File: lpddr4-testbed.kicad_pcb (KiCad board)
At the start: 6 copper layers, 69.6 x 30 mm, 68 parts, among them IC1 PCA96408APW, IC2 AT24CS01, J1 ddr4-sodimm-edge-connector, U1 MT53E1G32D2NP-046, U2 TPS613221ADBVT

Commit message: Replace broken component -PCA6408APW
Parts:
- IC1: value PCA96408APW -> PCA6408APW

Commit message: Migrate to KiCad 6
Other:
- net class Default removed

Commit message: Clean DRC
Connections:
- IC1 pad 11: Net-(IC1-Pad11) -> unconnected-(IC1-Pad11)
- IC1 pad 12: Net-(IC1-Pad12) -> unconnected-(IC1-Pad12)
- IC1 pad 13: Net-(IC1-Pad13) -> unconnected-(IC1-Pad13)
- J1 pad 100: Net-(J1-Pad100) -> unconnected-(J1-Pad100)
- J1 pad 102: Net-(J1-Pad102) -> unconnected-(J1-Pad102)
- J1 pad 104: Net-(J1-Pad104) -> unconnected-(J1-Pad104)
- J1 pad 106: Net-(J1-Pad106) -> unconnected-(J1-Pad106)
- J1 pad 108: Net-(J1-Pad108) -> unconnected-(J1-Pad108)
- J1 pad 109: Net-(J1-Pad109) -> unconnected-(J1-Pad109)
- J1 pad 110: Net-(J1-Pad110) -> unconnected-(J1-Pad110)
- J1 pad 111: Net-(J1-Pad111) -> unconnected-(J1-Pad111)
- J1 pad 112: Net-(J1-Pad112) -> unconnected-(J1-Pad112)
- J1 pad 113: Net-(J1-Pad113) -> unconnected-(J1-Pad113)
- J1 pad 114: Net-(J1-Pad114) -> unconnected-(J1-Pad114)
- J1 pad 115: Net-(J1-Pad115) -> unconnected-(J1-Pad115)
- J1 pad 117: Net-(J1-Pad117) -> unconnected-(J1-Pad117)
- J1 pad 119: Net-(J1-Pad119) -> unconnected-(J1-Pad119)
- J1 pad 121: Net-(J1-Pad121) -> unconnected-(J1-Pad121)
- J1 pad 123: Net-(J1-Pad123) -> unconnected-(J1-Pad123)
- J1 pad 125: Net-(J1-Pad125) -> unconnected-(J1-Pad125)
- J1 pad 131: Net-(J1-Pad131) -> unconnected-(J1-Pad131)
- J1 pad 132: Net-(J1-Pad132) -> unconnected-(J1-Pad132)
- J1 pad 133: Net-(J1-Pad133) -> unconnected-(J1-Pad133)
- J1 pad 134: Net-(J1-Pad134) -> unconnected-(J1-Pad134)
- J1 pad 135: Net-(J1-Pad135) -> unconnected-(J1-Pad135)
- J1 pad 136: Net-(J1-Pad136) -> unconnected-(J1-Pad136)
- J1 pad 137: Net-(J1-Pad137) -> unconnected-(J1-Pad137)
- J1 pad 138: Net-(J1-Pad138) -> unconnected-(J1-Pad138)
- J1 pad 139: Net-(J1-Pad139) -> unconnected-(J1-Pad139)
- J1 pad 140: Net-(J1-Pad140) -> unconnected-(J1-Pad140)
- J1 pad 141: Net-(J1-Pad141) -> unconnected-(J1-Pad141)
- J1 pad 142: Net-(J1-Pad142) -> unconnected-(J1-Pad142)
- J1 pad 143: Net-(J1-Pad143) -> unconnected-(J1-Pad143)
- J1 pad 144: Net-(J1-Pad144) -> unconnected-(J1-Pad144)
- J1 pad 145: Net-(J1-Pad145) -> unconnected-(J1-Pad145)
- J1 pad 146: Net-(J1-Pad146) -> unconnected-(J1-Pad146)
- J1 pad 147: Net-(J1-Pad147) -> unconnected-(J1-Pad147)
- J1 pad 148: Net-(J1-Pad148) -> unconnected-(J1-Pad148)
- J1 pad 149: Net-(J1-Pad149) -> unconnected-(J1-Pad149)
- J1 pad 150: Net-(J1-Pad150) -> unconnected-(J1-Pad150)
- J1 pad 151: Net-(J1-Pad151) -> unconnected-(J1-Pad151)
- J1 pad 152: Net-(J1-Pad152) -> unconnected-(J1-Pad152)
- J1 pad 153: Net-(J1-Pad153) -> unconnected-(J1-Pad153)
- J1 pad 155: Net-(J1-Pad155) -> unconnected-(J1-Pad155)
- J1 pad 157: Net-(J1-Pad157) -> unconnected-(J1-Pad157)
- J1 pad 159: Net-(J1-Pad159) -> unconnected-(J1-Pad159)
- J1 pad 170: Net-(J1-Pad170) -> unconnected-(J1-Pad170)
- J1 pad 172: Net-(J1-Pad172) -> unconnected-(J1-Pad172)
- J1 pad 174: Net-(J1-Pad174) -> unconnected-(J1-Pad174)
- J1 pad 176: Net-(J1-Pad176) -> unconnected-(J1-Pad176)
- J1 pad 178: Net-(J1-Pad178) -> unconnected-(J1-Pad178)
- J1 pad 180: Net-(J1-Pad180) -> unconnected-(J1-Pad180)
- J1 pad 182: Net-(J1-Pad182) -> unconnected-(J1-Pad182)
- J1 pad 188: Net-(J1-Pad188) -> unconnected-(J1-Pad188)
- J1 pad 190: Net-(J1-Pad190) -> unconnected-(J1-Pad190)
- J1 pad 198: Net-(J1-Pad198) -> unconnected-(J1-Pad198)
- J1 pad 202: Net-(J1-Pad202) -> unconnected-(J1-Pad202)
- J1 pad 208: Net-(J1-Pad208) -> unconnected-(J1-Pad208)
- J1 pad 212: Net-(J1-Pad212) -> unconnected-(J1-Pad212)
- J1 pad 213: Net-(J1-Pad213) -> unconnected-(J1-Pad213)
- J1 pad 214: Net-(J1-Pad214) -> unconnected-(J1-Pad214)
- J1 pad 215: Net-(J1-Pad215) -> unconnected-(J1-Pad215)
- J1 pad 216: Net-(J1-Pad216) -> unconnected-(J1-Pad216)
- J1 pad 217: Net-(J1-Pad217) -> unconnected-(J1-Pad217)
- J1 pad 218: Net-(J1-Pad218) -> unconnected-(J1-Pad218)
- J1 pad 219: Net-(J1-Pad219) -> unconnected-(J1-Pad219)
- J1 pad 220: Net-(J1-Pad220) -> unconnected-(J1-Pad220)
- J1 pad 221: Net-(J1-Pad221) -> unconnected-(J1-Pad221)
- J1 pad 222: Net-(J1-Pad222) -> unconnected-(J1-Pad222)
- J1 pad 223: Net-(J1-Pad223) -> unconnected-(J1-Pad223)
- J1 pad 224: Net-(J1-Pad224) -> unconnected-(J1-Pad224)
- J1 pad 225: Net-(J1-Pad225) -> unconnected-(J1-Pad225)
- J1 pad 226: Net-(J1-Pad226) -> unconnected-(J1-Pad226)
- J1 pad 227: Net-(J1-Pad227) -> unconnected-(J1-Pad227)
- J1 pad 228: Net-(J1-Pad228) -> unconnected-(J1-Pad228)
- J1 pad 229: Net-(J1-Pad229) -> unconnected-(J1-Pad229)
- J1 pad 230: Net-(J1-Pad230) -> unconnected-(J1-Pad230)
- J1 pad 231: Net-(J1-Pad231) -> unconnected-(J1-Pad231)
- J1 pad 232: Net-(J1-Pad232) -> unconnected-(J1-Pad232)
- J1 pad 233: Net-(J1-Pad233) -> unconnected-(J1-Pad233)
- J1 pad 234: Net-(J1-Pad234) -> unconnected-(J1-Pad234)
- J1 pad 235: Net-(J1-Pad235) -> unconnected-(J1-Pad235)
- J1 pad 236: Net-(J1-Pad236) -> unconnected-(J1-Pad236)
- J1 pad 237: Net-(J1-Pad237) -> unconnected-(J1-Pad237)
- J1 pad 238: Net-(J1-Pad238) -> unconnected-(J1-Pad238)
- J1 pad 239: Net-(J1-Pad239) -> unconnected-(J1-Pad239)
- J1 pad 240: Net-(J1-Pad240) -> unconnected-(J1-Pad240)
- J1 pad 241: Net-(J1-Pad241) -> unconnected-(J1-Pad241)
- J1 pad 242: Net-(J1-Pad242) -> unconnected-(J1-Pad242)
- J1 pad 243: Net-(J1-Pad243) -> unconnected-(J1-Pad243)
- J1 pad 244: Net-(J1-Pad244) -> unconnected-(J1-Pad244)
- J1 pad 245: Net-(J1-Pad245) -> unconnected-(J1-Pad245)
- J1 pad 247: Net-(J1-Pad247) -> unconnected-(J1-Pad247)
- J1 pad 249: Net-(J1-Pad249) -> unconnected-(J1-Pad249)
- J1 pad 251: Net-(J1-Pad251) -> unconnected-(J1-Pad251)
- J1 pad 252: Net-(J1-Pad252) -> unconnected-(J1-Pad252)
- J1 pad 253: Net-(J1-Pad253) -> unconnected-(J1-Pad253)
- J1 pad 254: Net-(J1-Pad254) -> unconnected-(J1-Pad254)
- J1 pad 255: Net-(J1-Pad255) -> unconnected-(J1-Pad255)
- J1 pad 256: Net-(J1-Pad256) -> unconnected-(J1-Pad256)
- J1 pad 257: Net-(J1-Pad257) -> unconnected-(J1-Pad257)
- J1 pad 258: Net-(J1-Pad258) -> unconnected-(J1-Pad258)
- J1 pad 259: Net-(J1-Pad259) -> unconnected-(J1-Pad259)
- J1 pad 260: Net-(J1-Pad260) -> unconnected-(J1-Pad260)
- J1 pad 51: Net-(J1-Pad51) -> unconnected-(J1-Pad51)
- J1 pad 52: Net-(J1-Pad52) -> unconnected-(J1-Pad52)
- J1 pad 53: Net-(J1-Pad53) -> unconnected-(J1-Pad53)
- J1 pad 54: Net-(J1-Pad54) -> unconnected-(J1-Pad54)
- J1 pad 55: Net-(J1-Pad55) -> unconnected-(J1-Pad55)
- J1 pad 56: Net-(J1-Pad56) -> unconnected-(J1-Pad56)
- J1 pad 57: Net-(J1-Pad57) -> unconnected-(J1-Pad57)
- J1 pad 58: Net-(J1-Pad58) -> unconnected-(J1-Pad58)
- J1 pad 59: Net-(J1-Pad59) -> unconnected-(J1-Pad59)
- J1 pad 60: Net-(J1-Pad60) -> unconnected-(J1-Pad60)
- J1 pad 61: Net-(J1-Pad61) -> unconnected-(J1-Pad61)
- J1 pad 62: Net-(J1-Pad62) -> unconnected-(J1-Pad62)
- J1 pad 63: Net-(J1-Pad63) -> unconnected-(J1-Pad63)
- J1 pad 64: Net-(J1-Pad64) -> unconnected-(J1-Pad64)
- J1 pad 65: Net-(J1-Pad65) -> unconnected-(J1-Pad65)
- J1 pad 66: Net-(J1-Pad66) -> unconnected-(J1-Pad66)
- J1 pad 67: Net-(J1-Pad67) -> unconnected-(J1-Pad67)
- J1 pad 68: Net-(J1-Pad68) -> unconnected-(J1-Pad68)
- J1 pad 69: Net-(J1-Pad69) -> unconnected-(J1-Pad69)
- J1 pad 70: Net-(J1-Pad70) -> unconnected-(J1-Pad70)
- J1 pad 71: Net-(J1-Pad71) -> unconnected-(J1-Pad71)
- J1 pad 72: Net-(J1-Pad72) -> unconnected-(J1-Pad72)
- J1 pad 73: Net-(J1-Pad73) -> unconnected-(J1-Pad73)
- J1 pad 74: Net-(J1-Pad74) -> unconnected-(J1-Pad74)
- J1 pad 75: Net-(J1-Pad75) -> unconnected-(J1-Pad75)
- J1 pad 76: Net-(J1-Pad76) -> unconnected-(J1-Pad76)
- J1 pad 77: Net-(J1-Pad77) -> unconnected-(J1-Pad77)
- J1 pad 78: Net-(J1-Pad78) -> unconnected-(J1-Pad78)
- J1 pad 79: Net-(J1-Pad79) -> unconnected-(J1-Pad79)
- J1 pad 80: Net-(J1-Pad80) -> unconnected-(J1-Pad80)
- J1 pad 81: Net-(J1-Pad81) -> unconnected-(J1-Pad81)
- J1 pad 82: Net-(J1-Pad82) -> unconnected-(J1-Pad82)
- J1 pad 83: Net-(J1-Pad83) -> unconnected-(J1-Pad83)
- J1 pad 84: Net-(J1-Pad84) -> unconnected-(J1-Pad84)
- J1 pad 85: Net-(J1-Pad85) -> unconnected-(J1-Pad85)
- J1 pad 86: Net-(J1-Pad86) -> unconnected-(J1-Pad86)
- J1 pad 87: Net-(J1-Pad87) -> unconnected-(J1-Pad87)
- J1 pad 88: Net-(J1-Pad88) -> unconnected-(J1-Pad88)
- J1 pad 89: Net-(J1-Pad89) -> unconnected-(J1-Pad89)
- J1 pad 90: Net-(J1-Pad90) -> unconnected-(J1-Pad90)
- J1 pad 91: Net-(J1-Pad91) -> unconnected-(J1-Pad91)
- J1 pad 92: Net-(J1-Pad92) -> unconnected-(J1-Pad92)
- J1 pad 94: Net-(J1-Pad94) -> unconnected-(J1-Pad94)
- J1 pad 96: Net-(J1-Pad96) -> unconnected-(J1-Pad96)
- J1 pad 98: Net-(J1-Pad98) -> unconnected-(J1-Pad98)
- U1 pad A1: Net-(U1-PadA1) -> unconnected-(U1-PadA1)
- U1 pad A11: Net-(U1-PadA11) -> unconnected-(U1-PadA11)
- U1 pad A12: Net-(U1-PadA12) -> unconnected-(U1-PadA12)
- U1 pad A2: Net-(U1-PadA2) -> unconnected-(U1-PadA2)
- U1 pad A8: Net-(U1-PadA8) -> unconnected-(U1-PadA8)
- U1 pad AA1: Net-(U1-PadAA1) -> unconnected-(U1-PadAA1)
- U1 pad AA11: Net-(U1-PadAA11) -> unconnected-(U1-PadAA11)
- U1 pad AA12: Net-(U1-PadAA12) -> unconnected-(U1-PadAA12)
- U1 pad AA2: Net-(U1-PadAA2) -> unconnected-(U1-PadAA2)
- U1 pad AA4: Net-(U1-PadAA4) -> unconnected-(U1-PadAA4)
- U1 pad AA9: Net-(U1-PadAA9) -> unconnected-(U1-PadAA9)
- U1 pad AB1: Net-(U1-PadAB1) -> unconnected-(U1-PadAB1)
- U1 pad AB11: Net-(U1-PadAB11) -> unconnected-(U1-PadAB11)
- U1 pad AB12: Net-(U1-PadAB12) -> unconnected-(U1-PadAB12)
- U1 pad AB2: Net-(U1-PadAB2) -> unconnected-(U1-PadAB2)
- U1 pad B1: Net-(U1-PadB1) -> unconnected-(U1-PadB1)
- U1 pad B12: Net-(U1-PadB12) -> unconnected-(U1-PadB12)
- U1 pad G11: Net-(U1-PadG11) -> unconnected-(U1-PadG11)
- U1 pad H3: Net-(U1-PadH3) -> unconnected-(U1-PadH3)
- U1 pad J5: Net-(U1-PadJ5) -> unconnected-(U1-PadJ5)
- U1 pad K5: Net-(U1-PadK5) -> unconnected-(U1-PadK5)
- U1 pad K8: Net-(U1-PadK8) -> unconnected-(U1-PadK8)
- U1 pad N5: Net-(U1-PadN5) -> unconnected-(U1-PadN5)
- U1 pad N8: Net-(U1-PadN8) -> unconnected-(U1-PadN8)
- U1 pad P11: Net-(U1-PadP11) -> unconnected-(U1-PadP11)
- U1 pad P2: Net-(U1-PadP2) -> unconnected-(U1-PadP2)
- U1 pad P4: Net-(U1-PadP4) -> unconnected-(U1-PadP4)
- U1 pad P5: Net-(U1-PadP5) -> unconnected-(U1-PadP5)
- U1 pad P8: Net-(U1-PadP8) -> unconnected-(U1-PadP8)
- U1 pad P9: Net-(U1-PadP9) -> unconnected-(U1-PadP9)
- U1 pad R10: Net-(U1-PadR10) -> unconnected-(U1-PadR10)
- U1 pad R11: Net-(U1-PadR11) -> unconnected-(U1-PadR11)
- U1 pad R2: Net-(U1-PadR2) -> unconnected-(U1-PadR2)
- U1 pad R3: Net-(U1-PadR3) -> unconnected-(U1-PadR3)
- U1 pad R9: Net-(U1-PadR9) -> unconnected-(U1-PadR9)
- U1 pad U11: Net-(U1-PadU11) -> unconnected-(U1-PadU11)
- U1 pad U2: Net-(U1-PadU2) -> unconnected-(U1-PadU2)
- U1 pad U4: Net-(U1-PadU4) -> unconnected-(U1-PadU4)
- U1 pad U9: Net-(U1-PadU9) -> unconnected-(U1-PadU9)
- U1 pad V10: Net-(U1-PadV10) -> unconnected-(U1-PadV10)
- U1 pad V11: Net-(U1-PadV11) -> unconnected-(U1-PadV11)
- U1 pad V2: Net-(U1-PadV2) -> unconnected-(U1-PadV2)
- U1 pad V3: Net-(U1-PadV3) -> unconnected-(U1-PadV3)
- U1 pad V4: Net-(U1-PadV4) -> unconnected-(U1-PadV4)
- U1 pad V9: Net-(U1-PadV9) -> unconnected-(U1-PadV9)
- U1 pad W10: Net-(U1-PadW10) -> unconnected-(U1-PadW10)
- U1 pad W3: Net-(U1-PadW3) -> unconnected-(U1-PadW3)
- U1 pad Y10: Net-(U1-PadY10) -> unconnected-(U1-PadY10)
- U1 pad Y11: Net-(U1-PadY11) -> unconnected-(U1-PadY11)
- U1 pad Y2: Net-(U1-PadY2) -> unconnected-(U1-PadY2)
- U1 pad Y3: Net-(U1-PadY3) -> unconnected-(U1-PadY3)
- U1 pad Y4: Net-(U1-PadY4) -> unconnected-(U1-PadY4)
- U1 pad Y9: Net-(U1-PadY9) -> unconnected-(U1-PadY9)
- U2 pad 3: Net-(U2-Pad3) -> unconnected-(U2-Pad3)
- U2 pad 5: Net-(U2-Pad5) -> unconnected-(U2-Pad5)
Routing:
- net VDDQ: track 44.7 -> 39.1 mm
- net VDD2: track 57.0 -> 55.6 mm
- net GND: track 237.4 -> 236.3 mm
- net VDD1: track 100.3 -> 100.2 mm, vias 19 -> 18

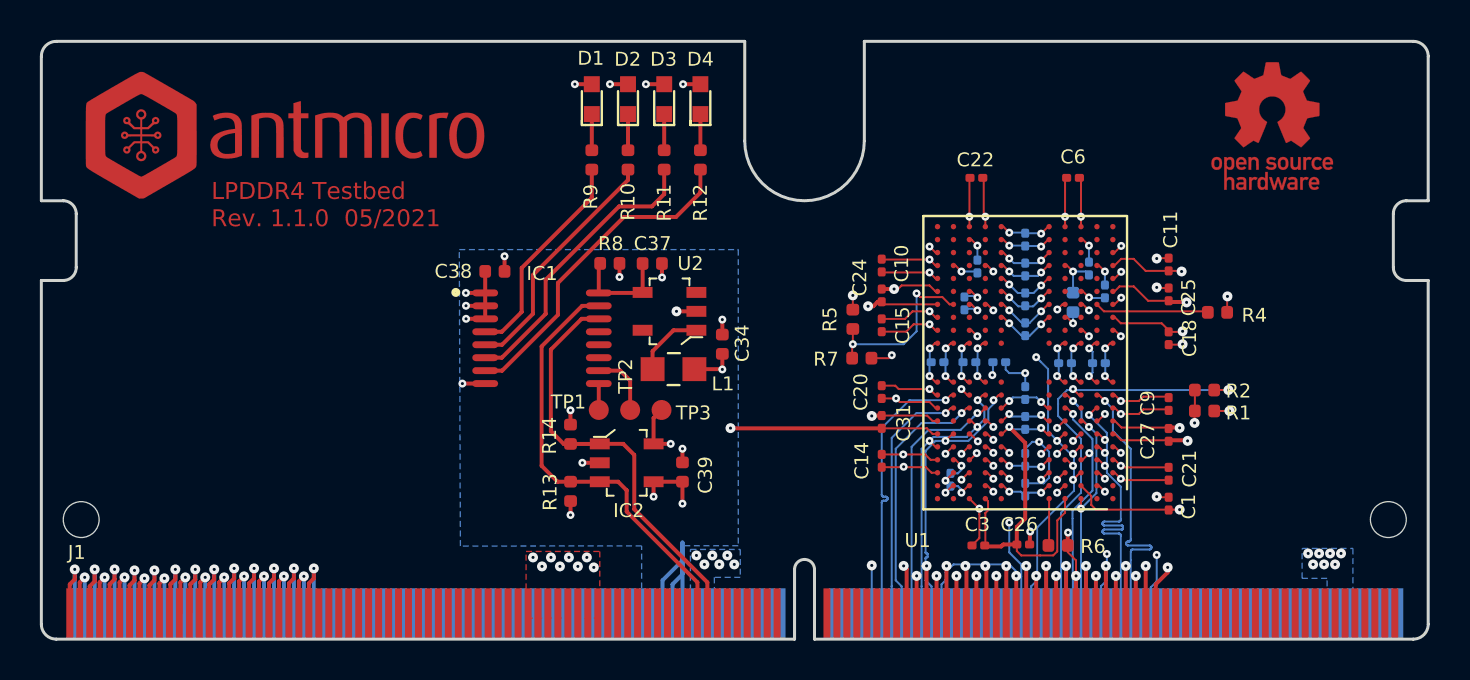
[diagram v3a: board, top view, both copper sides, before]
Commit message: Replace burried vias with regular vias
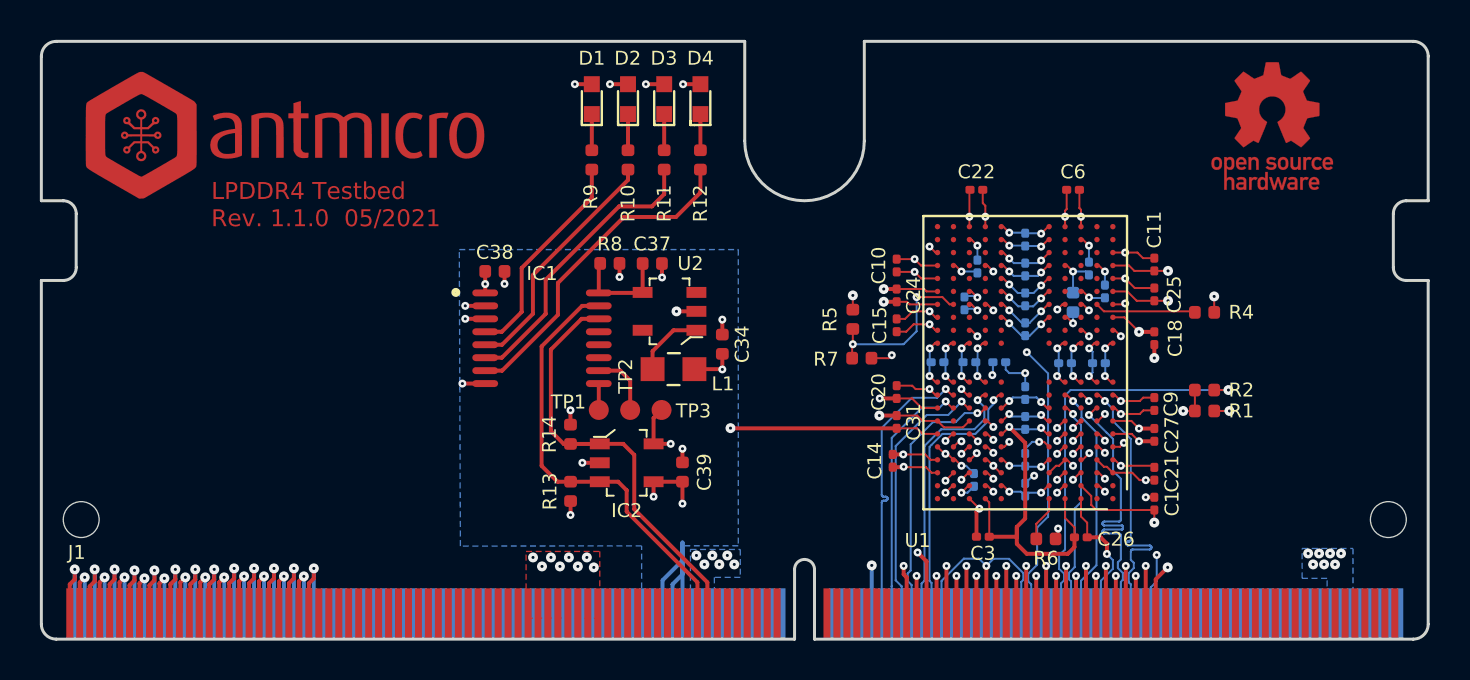
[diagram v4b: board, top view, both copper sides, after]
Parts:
- moved C26 2.91 mm to (152.2, 94.9)
- moved C7 1.18 mm to (146.8, 92.0)
- moved C10 0.75 mm to (142.9, 81.2)
- moved C15 0.75 mm to (142.9, 84.2)
- moved C20 0.75 mm to (142.9, 87.6)
- moved C24 0.75 mm to (142.9, 82.8)
- moved C31 0.75 mm to (142.9, 89.1)
- moved C1 0.72 mm to (155.9, 93.2)
- moved C11 0.72 mm to (155.9, 81.2)
- moved C18 0.72 mm to (155.9, 84.9)
- moved C21 0.72 mm to (155.9, 91.7)
- moved C25 0.72 mm to (155.9, 82.7)
- moved C27 0.72 mm to (155.9, 89.8)
- moved C9 0.72 mm to (155.9, 88.2)
- moved R6 0.69 mm to (150.4, 95.0)
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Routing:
- net VDD1: track 100.2 -> 89.8 mm
- net GND: track 236.3 -> 229.1 mm, vias 111 -> 102
- net VDD2: track 55.6 -> 51.7 mm
- net VDDQ: track 39.1 -> 35.8 mm
- net DQ06_A: track 10.7 -> 9.44 mm
- net DQ10_A: track 10.7 -> 12.0 mm
- net RESET_N: track 22.7 -> 21.8 mm
- net OTD_CA_A: track 21.1 -> 20.2 mm
- net Net-(R1-Pad2): track 7.35 -> 6.61 mm
- net Net-(R4-Pad2): track 5.73 -> 5.08 mm
- net DQ11_A: track 10.7 -> 10.1 mm
- net DQ04_A: track 10.7 -> 10.1 mm

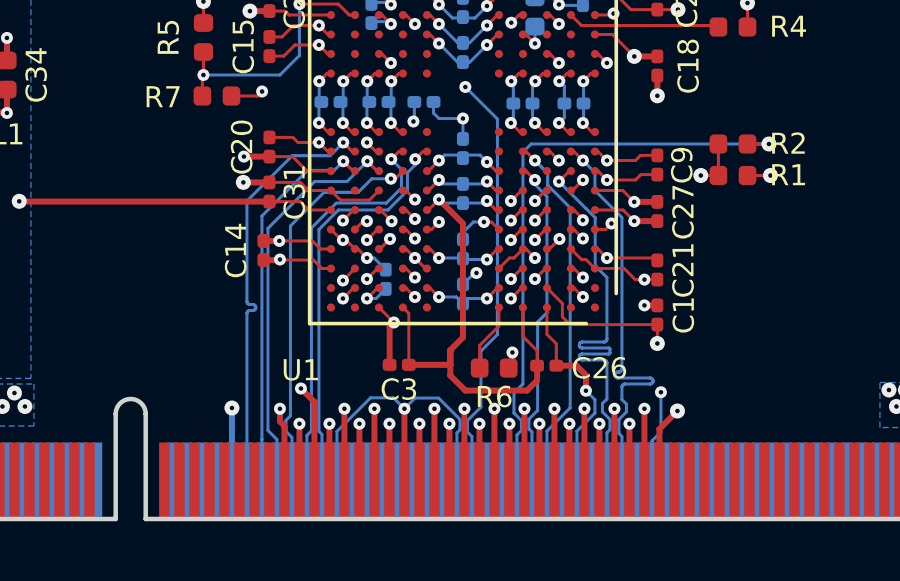
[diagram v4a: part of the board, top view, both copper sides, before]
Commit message: Fix net names
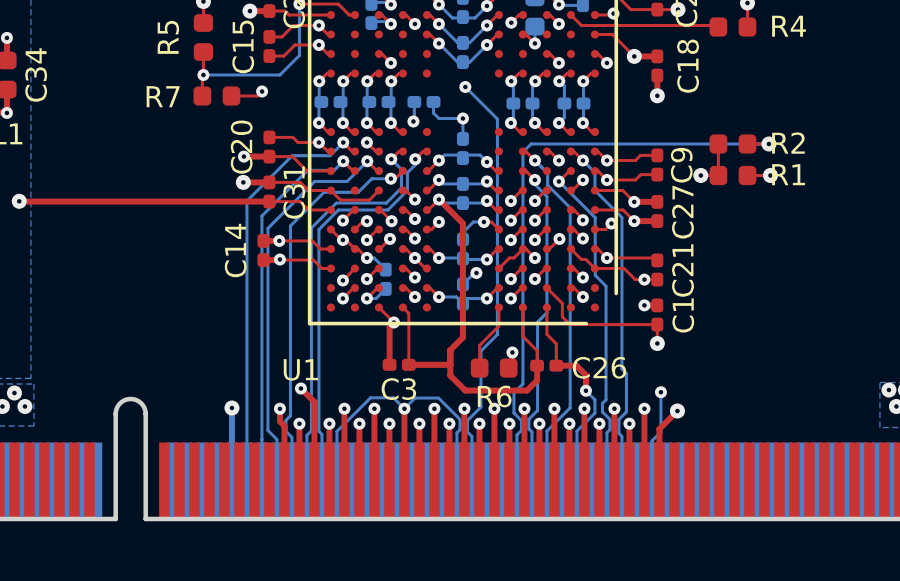
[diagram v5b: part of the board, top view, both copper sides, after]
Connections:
- net CA_0A renamed CA0_A
- net CA_1A renamed CA1_A
- net CK_CA renamed CK_C_A
- net CK_TA renamed CK_T_A
- net OTD_CA_A renamed ODT_CA_A
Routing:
- net CA0_A: track 15.0 -> 11.3 mm
- net CA1_A: track 14.2 -> 11.9 mm

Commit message: Length matching
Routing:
- net CS0_A: track 11.0 -> 14.1 mm
- net DQ_S0_TA: track 13.0 -> 10.2 mm
- net CA0_A: track 11.3 -> 14.1 mm
- net DQ13_A: track 12.7 -> 10.2 mm
- net CA1_A: track 11.9 -> 14.1 mm
- net DQ10_A: track 12.0 -> 10.2 mm
- net CKE0_A: track 12.5 -> 14.1 mm
- net CA4_A: track 12.8 -> 14.1 mm
- net CA2_A: track 13.1 -> 14.1 mm
- net CA3_A: track 13.3 -> 14.1 mm
- net DQ06_A: track 9.44 -> 10.2 mm
- net CK_T_A: track 13.5 -> 14.1 mm
- net DQ09_A: track 10.8 -> 10.2 mm
- net CK_C_A: track 13.6 -> 14.2 mm
- net DQ07_A: track 10.7 -> 10.2 mm
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
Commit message: Bump revision to 1.2.0
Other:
- board text added: "LPDDR4 Testbed Rev. 1.2.0 12/2022"
- board text removed: "LPDDR4 Testbed Rev. 1.1.0 05/2021"
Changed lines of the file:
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@@
   (gr_line (start 135.3 75) (end 135.3 70) (layer "Edge.Cuts") (width 0.15))
   (gr_line (start 169.6 78) (end 169.600002 70.75) (layer "Edge.Cuts") (width 0.15))
-  (gr_text "LPDDR4 Testbed\nRev. 1.1.0  05/2021" (at 108.525 78.2) (layer "F.Cu")
+  (gr_text "LPDDR4 Testbed\nRev. 1.2.0  12/2022" (at 108.525 78.2) (layer "F.Cu")
     (effects (font (size 0.85 0.85) (thickness 0.18)) (justify left))
   )
-  (gr_text "LPDDR4 Testbed\nRev. 1.1.0  05/2021" (at 108.525 78.2) (layer "F.Mask")
+  (gr_text "LPDDR4 Testbed\nRev. 1.2.0  12/2022" (at 108.525 78.2) (layer "F.Mask")
     (effects (font (size 0.85 0.85) (thickness 0.18)) (justify left))
   )
